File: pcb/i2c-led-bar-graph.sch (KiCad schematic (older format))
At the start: 0 parts

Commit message: Add all components to schematic
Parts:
- added D? (x10): Led_Small, symbol Led_Small
- added J?: I2C_RJ14, symbol I2C_RJ14
- added U?: MCP23017, symbol MCP23017
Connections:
- new net: J?.3 (SDA), U?.13 (SDA)
- new net: J?.4 (SCL), U?.12 (SCL)
- new net VDD: J?.1 (VDD), U?.18 (~RESET), U?.9 (VDD)
- new net VSS: J?.2 (VSS), U?.10 (VSS)
- no-connect marks 0 -> 2
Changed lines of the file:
@@
 Comment4 ""
 $EndDescr
+$Comp
+L I2C_RJ14 J?
+U 1 1 55435B19
+P 1600 2150
+F 0 "J?" H 2100 2950 60  0000 C CNN
+F 1 "I2C_RJ14" H 1750 2950 60  0000 C CNN
+F 2 "" H 3000 2550 60  0000 C CNN
+F 3 "" H 3000 2550 60  0000 C CNN
+	1    1600 2150
+	1    0    0    -1
+$EndComp
+$Comp
+L VDD #PWR?
+U 1 1 55435EFD
+P 2200 2400
+F 0 "#PWR?" H 2200 2250 50  0001 C CNN
+F 1 "VDD" H 2200 2550 50  0000 C CNN
+F 2 "" H 2200 2400 60  0000 C CNN
+F 3 "" H 2200 2400 60  0000 C CNN
+	1    2200 2400
+	0    1    1    0
+$EndComp
+$Comp
+L VSS #PWR?
+U 1 1 55435F18
+P 2000 2450
+F 0 "#PWR?" H 2000 2300 50  0001 C CNN
+F 1 "VSS" H 2000 2600 50  0000 C CNN
+F 2 "" H 2000 2450 60  0000 C CNN
+F 3 "" H 2000 2450 60  0000 C CNN
+	1    2000 2450
+	-1   0    0    1
+$EndComp
+Wire Wire Line
+	2150 2300 2150 2400
+Wire Wire Line
+	2150 2400 2200 2400
+Wire Wire Line
+	2000 2300 2000 2450
+$Comp
+L MCP23017 U?
+U 1 1 55436A35
+P 3650 2450
+F 0 "U?" H 3650 2450 60  0000 C CNN
+F 1 "MCP23017" H 3650 2600 60  0000 C CNN
+F 2 "" H 3650 2450 60  0000 C CNN
+F 3 "" H 3650 2450 60  0000 C CNN
+	1    3650 2450
+	1    0    0    -1
+$EndComp
+Wire Wire Line
+	1850 2300 1850 2900
+Wire Wire Line
+	1850 2900 2900 2900
+Wire Wire Line
+	2900 2800 1700 2800
+Wire Wire Line
+	1700 2800 1700 2300
+$Comp
+L VDD #PWR?
+U 1 1 55436B64
+P 2700 3100
+F 0 "#PWR?" H 2700 2950 50  0001 C CNN
+F 1 "VDD" H 2700 3250 50  0000 C CNN
+F 2 "" H 2700 3100 60  0000 C CNN
+F 3 "" H 2700 3100 60  0000 C CNN
+	1    2700 3100
+	0    -1   -1   0
+$EndComp
+$Comp
+L VDD #PWR?
+U 1 1 55436B7A
+P 3550 3650
+F 0 "#PWR?" H 3550 3500 50  0001 C CNN
+F 1 "VDD" H 3550 3800 50  0000 C CNN
+F 2 "" H 3550 3650 60  0000 C CNN
+F 3 "" H 3550 3650 60  0000 C CNN
+	1    3550 3650
+	-1   0    0    1
+$EndComp
+$Comp
+L VSS #PWR?
+U 1 1 55436B90
+P 3750 3650
+F 0 "#PWR?" H 3750 3500 50  0001 C CNN
+F 1 "VSS" H 3750 3800 50  0000 C CNN
+F 2 "" H 3750 3650 60  0000 C CNN
+F 3 "" H 3750 3650 60  0000 C CNN
+	1    3750 3650
+	-1   0    0    1
+$EndComp
+Wire Wire Line
+	3750 3500 3750 3650
+Wire Wire Line
+	3550 3500 3550 3650
+Wire Wire Line
+	2900 3100 2700 3100
+NoConn ~ 4400 2850
+NoConn ~ 4400 2750
+$Comp
+L Led_Small D?
+U 1 1 55436EA2
+P 5150 2700
+F 0 "D?" H 5100 2825 50  0000 L CNN
+F 1 "Led_Small" H 4975 2600 50  0001 L CNN
+F 2 "" V 5150 2700 60  0000 C CNN
+F 3 "" V 5150 2700 60  0000 C CNN
+	1    5150 2700
+	-1   0    0    1
+$EndComp
+$Comp
+L Led_Small D?
+U 1 1 55436F17
+P 5150 2500
+F 0 "D?" H 5100 2625 50  0000 L CNN
+F 1 "Led_Small" H 4975 2400 50  0001 L CNN
+F 2 "" V 5150 2500 60  0000 C CNN
+F 3 "" V 5150 2500 60  0000 C CNN
+	1    5150 2500
+	-1   0    0    1
+$EndComp
+$Comp
+L Led_Small D?
+U 1 1 55437029
+P 5150 2300
+F 0 "D?" H 5100 2425 50  0000 L CNN
+F 1 "Led_Small" H 4975 2200 50  0001 L CNN
+F 2 "" V 5150 2300 60  0000 C CNN
+F 3 "" V 5150 2300 60  0000 C CNN
+	1    5150 2300
+	-1   0    0    1
+$EndComp
+$Comp
+L Led_Small D?
+U 1 1 5543709E
+P 5150 2900
+F 0 "D?" H 5100 3025 50  0000 L CNN
+F 1 "Led_Small" H 4975 2800 50  0001 L CNN
+F 2 "" V 5150 2900 60  0000 C CNN
+F 3 "" V 5150 2900 60  0000 C CNN
+	1    5150 2900
+	-1   0    0    1
+$EndComp
+$Comp
+L Led_Small D?
+U 1 1 55437105
+P 5150 3100
+F 0 "D?" H 5100 3225 50  0000 L CNN
+F 1 "Led_Small" H 4975 3000 50  0001 L CNN
+F 2 "" V 5150 3100 60  0000 C CNN
+F 3 "" V 5150 3100 60  0000 C CNN
+	1    5150 3100
+	-1   0    0    1
+$EndComp
+$Comp
+L Led_Small D?
+U 1 1 55437123
+P 5150 2100
+F 0 "D?" H 5100 2225 50  0000 L CNN
+F 1 "Led_Small" H 4975 2000 50  0001 L CNN
+F 2 "" V 5150 2100 60  0000 C CNN
+F 3 "" V 5150 2100 60  0000 C CNN
+	1    5150 2100
+	-1   0    0    1
+$EndComp
+$Comp
+L Led_Small D?
+U 1 1 55437140
+P 5150 1900
+F 0 "D?" H 5100 2025 50  0000 L CNN
+F 1 "Led_Small" H 4975 1800 50  0001 L CNN
+F 2 "" V 5150 1900 60  0000 C CNN
+F 3 "" V 5150 1900 60  0000 C CNN
+	1    5150 1900
+	-1   0    0    1
+$EndComp
+$Comp
+L Led_Small D?
+U 1 1 5543715C
+P 5150 1500
+F 0 "D?" H 5100 1625 50  0000 L CNN
+F 1 "Led_Small" H 4975 1400 50  0001 L CNN
+F 2 "" V 5150 1500 60  0000 C CNN
+F 3 "" V 5150 1500 60  0000 C CNN
+	1    5150 1500
+	-1   0    0    1
+$EndComp
+$Comp
+L Led_Small D?
+U 1 1 55437179
+P 5150 1700
+F 0 "D?" H 5100 1825 50  0000 L CNN
+F 1 "Led_Small" H 4975 1600 50  0001 L CNN
+F 2 "" V 5150 1700 60  0000 C CNN
+F 3 "" V 5150 1700 60  0000 C CNN
+	1    5150 1700
+	-1   0    0    1
+$EndComp
+$Comp
+L Led_Small D?
+U 1 1 55437197
+P 5150 3300
+F 0 "D?" H 5100 3425 50  0000 L CNN
+F 1 "Led_Small" H 4975 3200 50  0001 L CNN
+F 2 "" V 5150 3300 60  0000 C CNN
+F 3 "" V 5150 3300 60  0000 C CNN
+	1    5150 3300
+	-1   0    0    1
+$EndComp
 $EndSCHEMATC

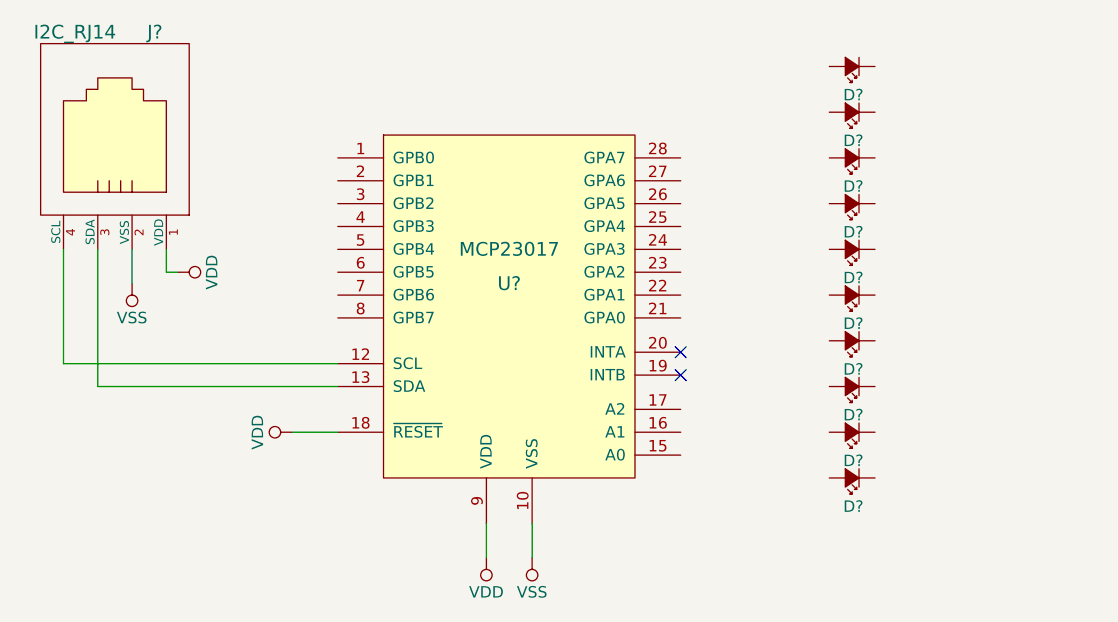
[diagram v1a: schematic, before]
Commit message: Add all components and connect with wires
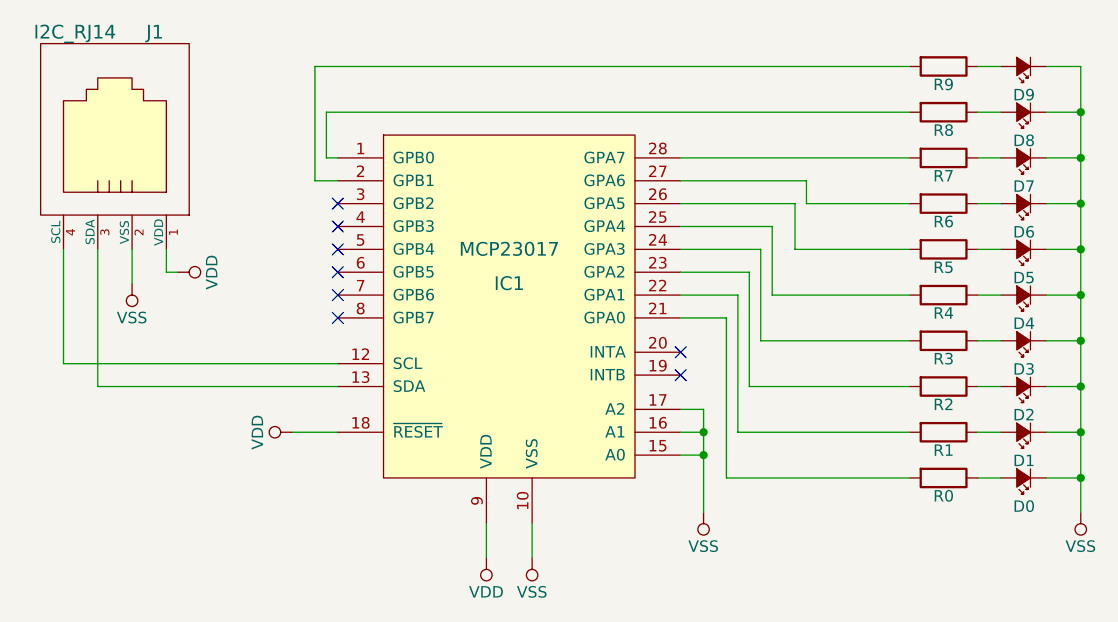
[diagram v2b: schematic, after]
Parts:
- added R0, R1, R2, R3, R4, R5, R6, R7, R8, R9: R, symbol R
- gave numbers to parts that had none: 12
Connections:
- net VSS: now also D0.1 (K), D1.1 (K), D2.1 (K), D3.1 (K), D4.1 (K), D5.1 (K), D6.1 (K), D7.1 (K), D8.1 (K), D9.1 (K), IC1.15 (A0), IC1.16 (A1), IC1.17 (A2)
- net at IC1.1 (GPB0): now also R8.2
- net at IC1.2 (GPB1): now also R9.2
- net at IC1.21 (GPA0): now also R0.2
- net at IC1.22 (GPA1): now also R1.2
- net at IC1.23 (GPA2): now also R2.2
- net at IC1.24 (GPA3): now also R3.2
- net at IC1.25 (GPA4): now also R4.2
- net at IC1.26 (GPA5): now also R5.2
- net at IC1.27 (GPA6): now also R6.2
- net at IC1.28 (GPA7): now also R7.2
- net at D3.2 (A): now also R3.1
- net at D4.2 (A): now also R4.1
- net at D5.2 (A): now also R5.1
- net at D2.2 (A): now also R2.1
- net at D1.2 (A): now also R1.1
- net at D6.2 (A): now also R6.1
- net at D7.2 (A): now also R7.1
- net at D9.2 (A): now also R9.1
- net at D8.2 (A): now also R8.1
- net at D0.2 (A): now also R0.1
- no-connect marks 2 -> 8
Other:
- moved on the sheet: D0, D1, D2, D3, D4, D5, D6, D7, D8, D9
